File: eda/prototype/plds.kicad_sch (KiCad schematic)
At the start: 3 parts, among them U17 GAL22V10, U2 GAL16V8, U9 GAL16V8

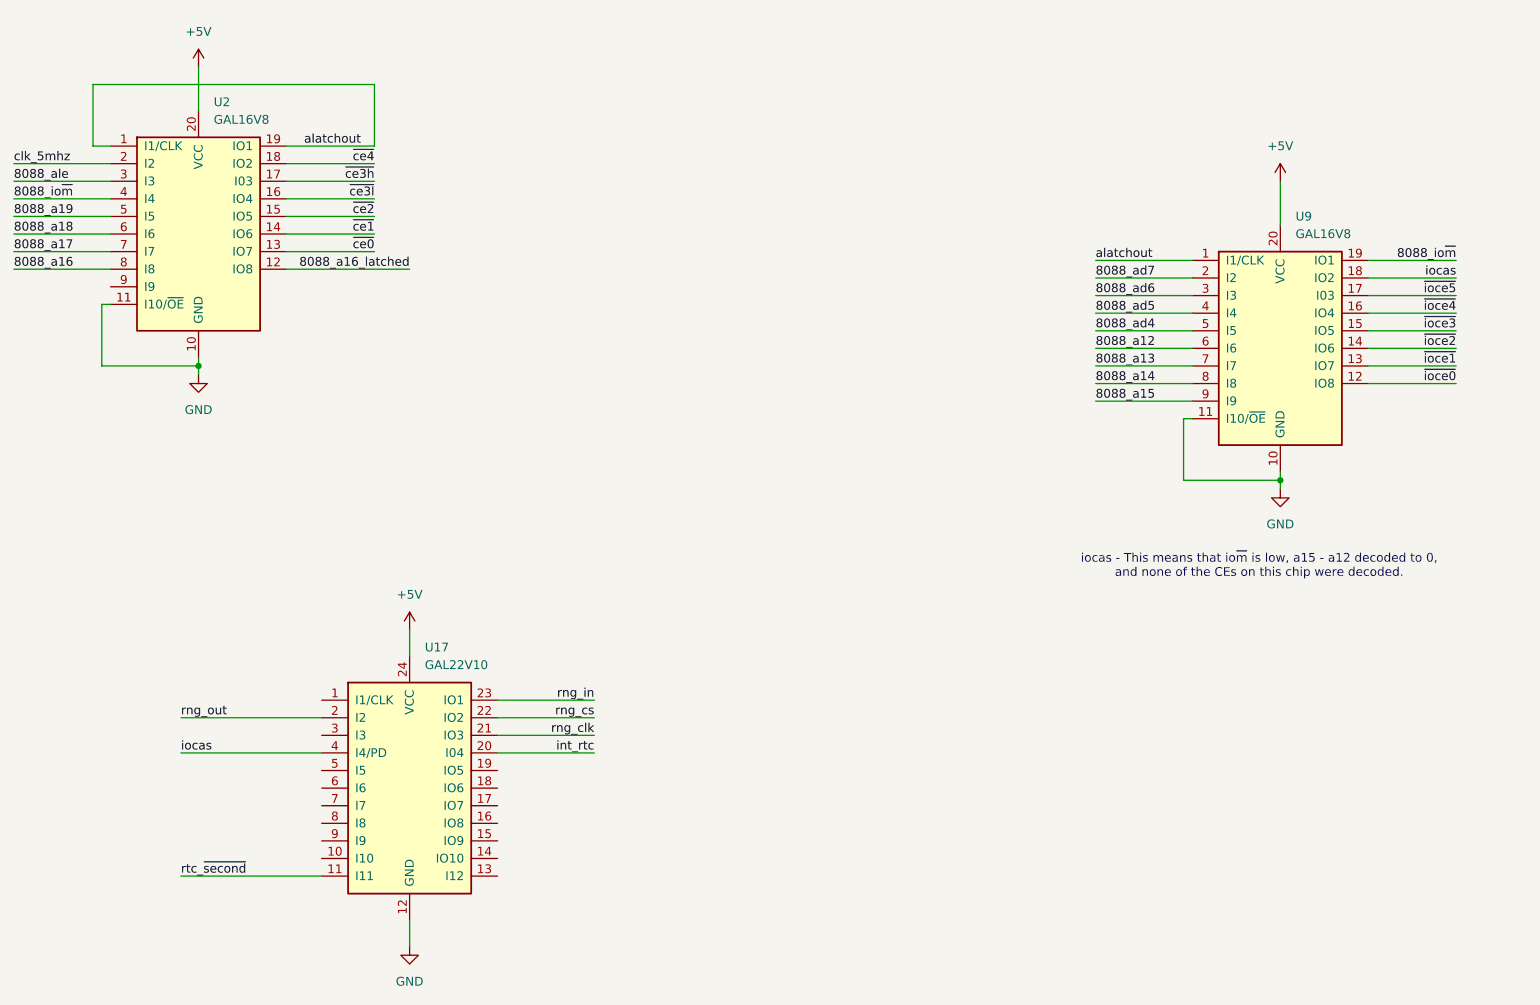
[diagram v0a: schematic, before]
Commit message: eda: prototype: Split up a bit, add RTC
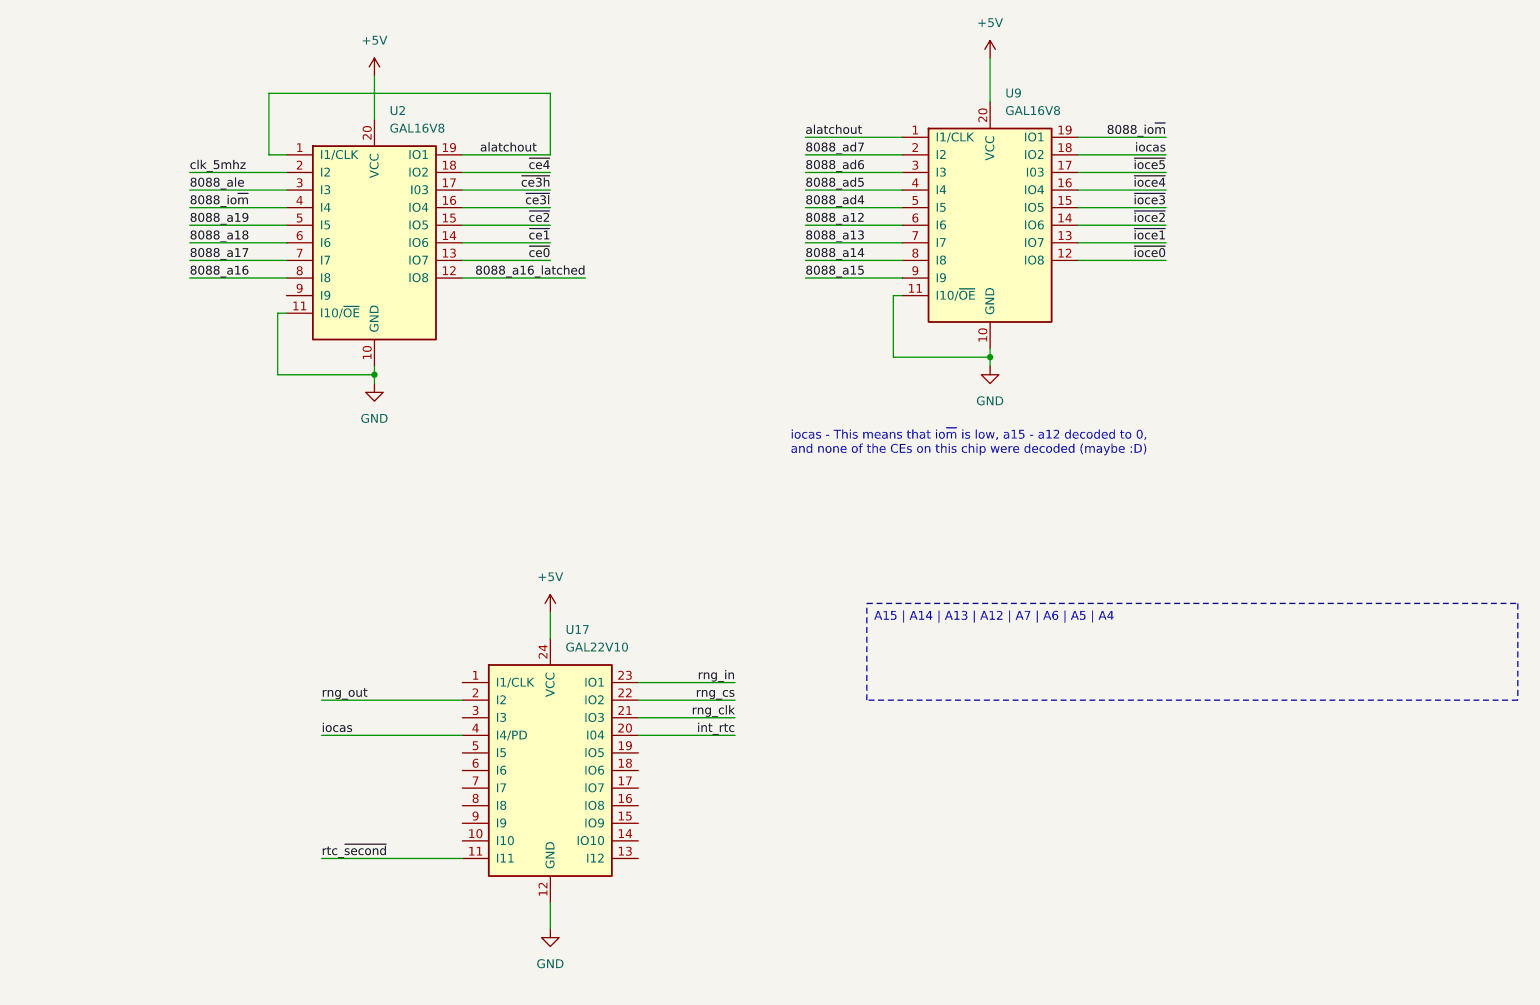
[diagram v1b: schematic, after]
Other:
- note added: "iocas - This means that io~{m} is low, a15 - a12 decoded to 0, and none of the CEs on this chip were decoded (maybe :D)"
- note removed: "iocas - This means that io~{m} is low, a15 - a12 decoded to 0, and none of the CEs on this chip were decoded."
- moved on the sheet: U17, U2, U9
